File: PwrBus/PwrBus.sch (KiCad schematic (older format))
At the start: 8 parts, among them J1 Screw_Terminal_01x02, J2 Screw_Terminal_01x02, J3 Screw_Terminal_01x02, J4 Screw_Terminal_01x02, J5 Screw_Terminal_01x02, J6 Screw_Terminal_01x02, J7 Screw_Terminal_01x02, Q1 IRLML5203

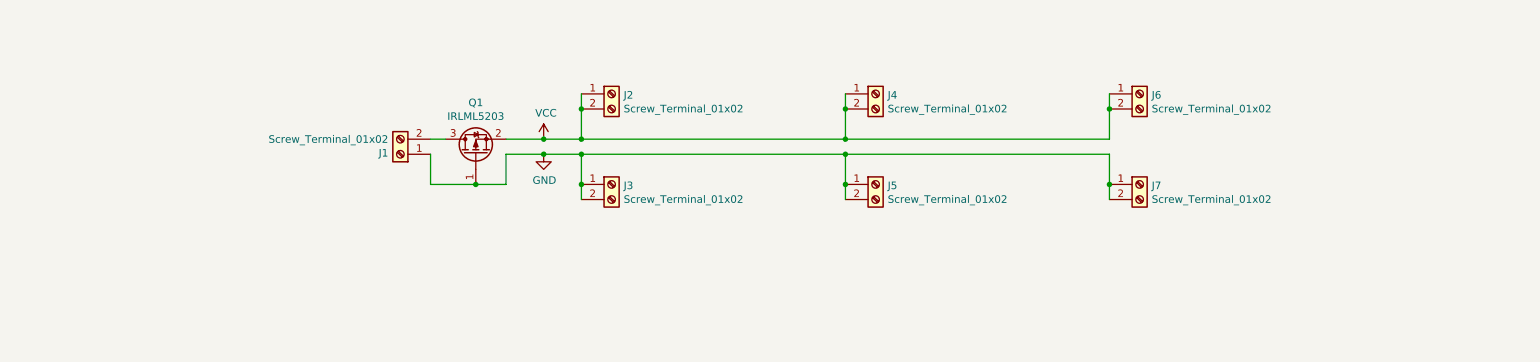
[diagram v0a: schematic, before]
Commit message: Move sockets
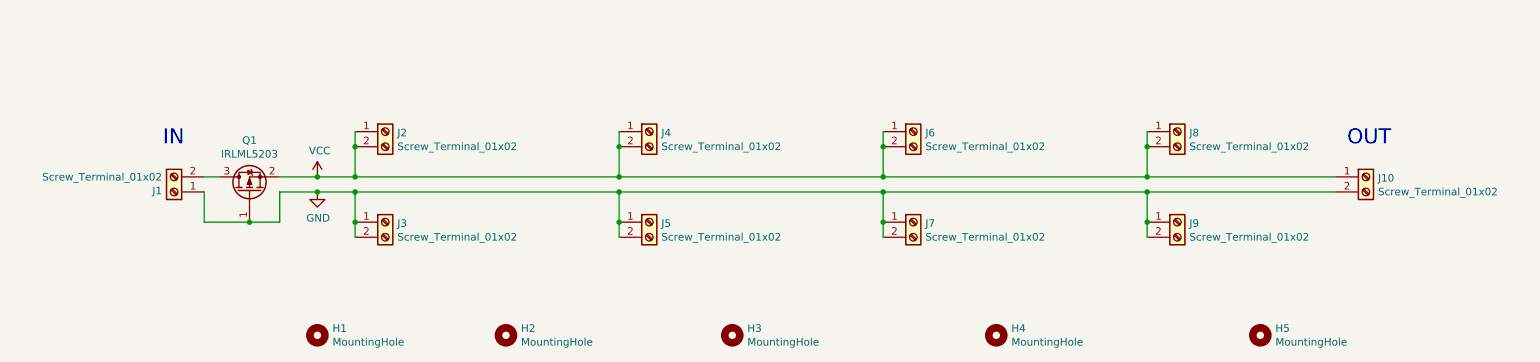
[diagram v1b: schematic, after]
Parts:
- added H1, H2, H3, H4, H5: MountingHole, MountingHole:MountingHole_3.2mm_M3, symbol Mechanical:MountingHole
- added J10, J8, J9: Screw_Terminal_01x02, TerminalBlock_Phoenix:TerminalBlock_Phoenix_MKDS-1,5-2_1x02_P5.00mm_Horizontal, symbol Connector:Screw_Terminal_01x02
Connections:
- net GND: now also J10.2 (Pin_2), J9.1 (Pin_1), J9.2 (Pin_2)
- net VCC: now also J10.1 (Pin_1), J8.1 (Pin_1), J8.2 (Pin_2)
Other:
- note added: "IN"
- note added: "OUT"
- moved on the sheet: J1, J2, J3, J4, J5, J6, J7, Q1

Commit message: Power bus is ready
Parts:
- added D1: LED, LED_THT:LED_D5.0mm, symbol Device:LED
- added R1: 1k, Resistor_SMD:R_0805_2012Metric_Pad1.20x1.40mm_HandSolder, symbol Device:R
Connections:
- net GND: now also D1.1 (K)
- net VCC: now also R1.1
- new net: D1.2 (A), R1.2
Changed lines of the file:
@@
 Connection ~ 2750 2700
 Wire Wire Line
-	2750 2800 4500 2800
+	2750 2800 4000 2800
 Wire Wire Line
 	4500 2800 4500 3000
@@
 Connection ~ 4500 3000
 Wire Wire Line
-	4500 2700 6250 2700
+	4500 2700 5750 2700
 Wire Wire Line
 	6250 2700 6250 2500
@@
 Text Notes 9325 2500 0    100  ~ 0
 OUT
+$Comp
+L Device:LED D1
+U 1 1 669C336A
+P 4350 1875
+F 0 "D1" H 4343 2092 50  0000 C CNN
+F 1 "LED" H 4343 2001 50  0000 C CNN
+F 2 "LED_THT:LED_D5.0mm" H 4350 1875 50  0001 C CNN
+F 3 "~" H 4350 1875 50  0001 C CNN
+	1    4350 1875
+	1    0    0    -1
+$EndComp
+$Comp
+L Device:R R1
+U 1 1 669C3987
+P 4650 1875
+F 0 "R1" V 4443 1875 50  0000 C CNN
+F 1 "1k" V 4534 1875 50  0000 C CNN
+F 2 "Resistor_SMD:R_0805_2012Metric_Pad1.20x1.40mm_HandSolder" V 4580 1875 50  0001 C CNN
+F 3 "~" H 4650 1875 50  0001 C CNN
+	1    4650 1875
+	0    1    1    0
+$EndComp
+Wire Wire Line
+	4800 1875 5750 1875
+Wire Wire Line
+	5750 1875 5750 2700
+Connection ~ 5750 2700
+Wire Wire Line
+	5750 2700 6250 2700
+Wire Wire Line
+	4200 1875 4000 1875
+Wire Wire Line
+	4000 1875 4000 2800
+Connection ~ 4000 2800
+Wire Wire Line
+	4000 2800 4500 2800
 $EndSCHEMATC
